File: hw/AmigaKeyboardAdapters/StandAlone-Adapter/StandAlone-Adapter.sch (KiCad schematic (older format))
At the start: 52 parts, among them J1 RJ10, J2 Conn_02x03_Odd_Even, P1 CONN_01X02, Q1 BSS138, Q2 BSS138, Q3 BSS138, U1 AZ1117-3.3, U3 STM32F401RCTx

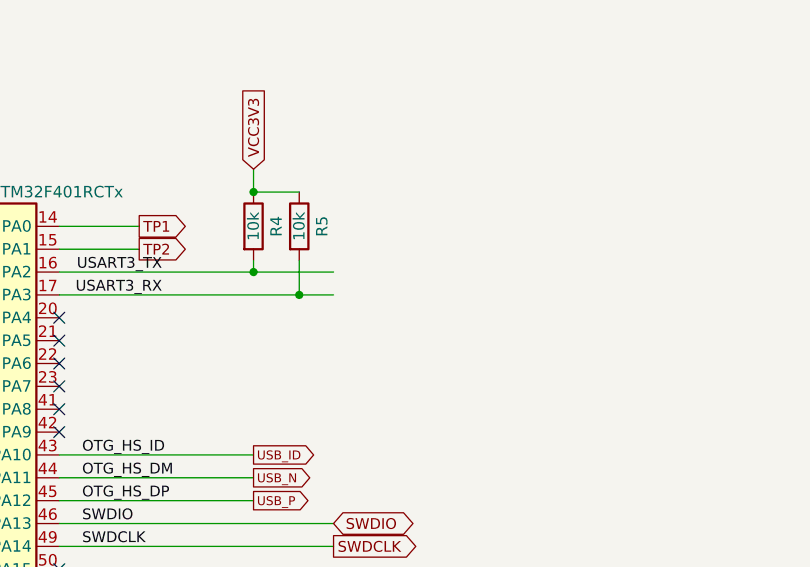
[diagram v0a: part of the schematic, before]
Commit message: The Debug UART Pins (RX & TX) were left unconnected
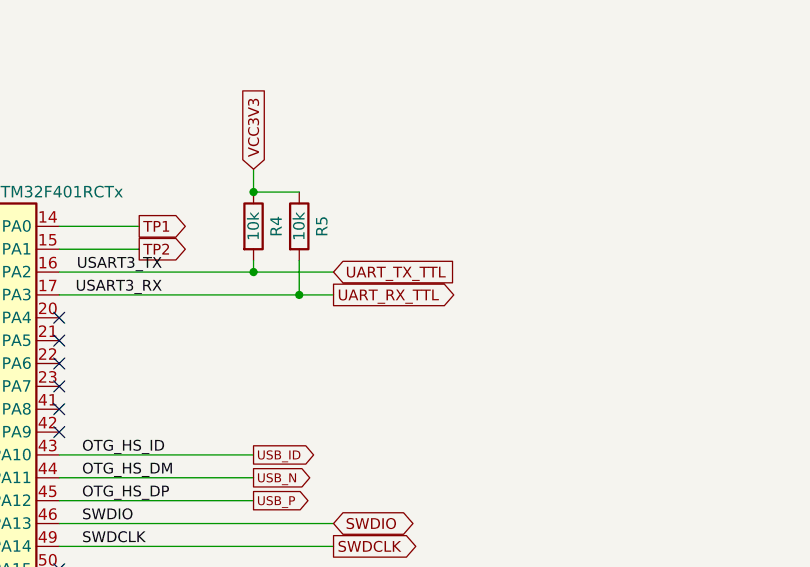
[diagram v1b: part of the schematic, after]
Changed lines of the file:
@@
 Wire Notes Line
 	10600 3600 10600 2600
+Text GLabel 10450 4800 2    47   Input ~ 0
+UART_TX_TTL
+Text GLabel 10450 4900 2    47   Output ~ 0
+UART_RX_TTL
 $EndSCHEMATC

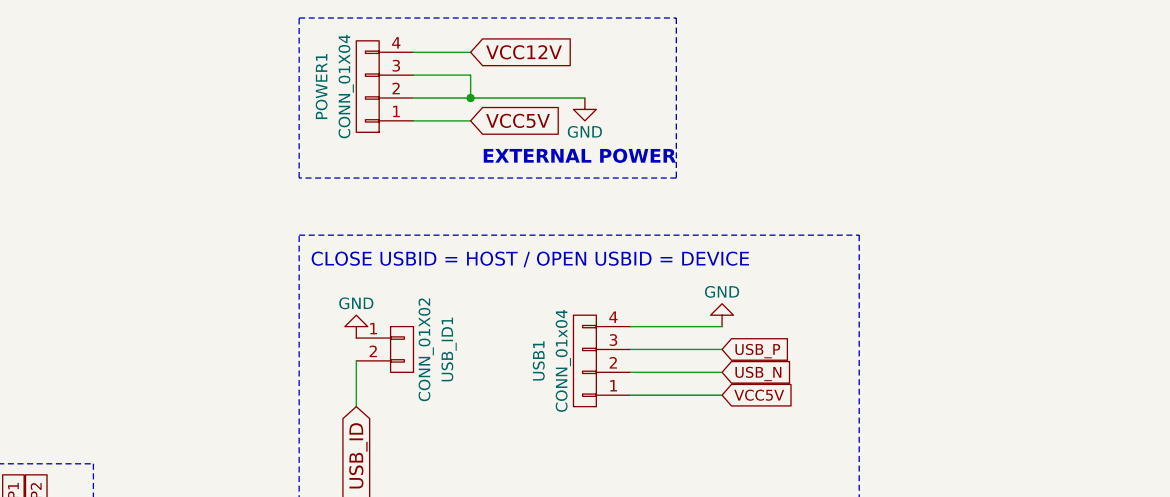
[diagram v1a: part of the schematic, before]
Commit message: Changed to reflect new path on my system
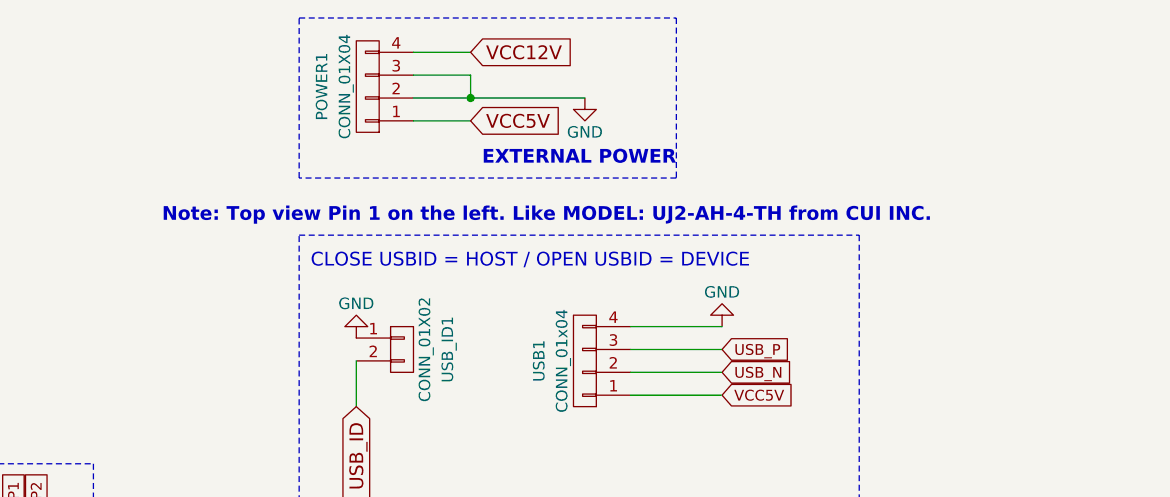
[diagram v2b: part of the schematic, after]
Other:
- note added: "Note: Top view Pin 1 on the left. Like MODEL: UJ2-AH-4-TH from CUI INC."
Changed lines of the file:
@@
 Text GLabel 10450 4900 2    47   Output ~ 0
 UART_RX_TTL
+Text Notes 12450 1550 0    60   ~ 12
+Note: Top view Pin 1 on the left. Like MODEL: UJ2-AH-4-TH from CUI INC.
 $EndSCHEMATC

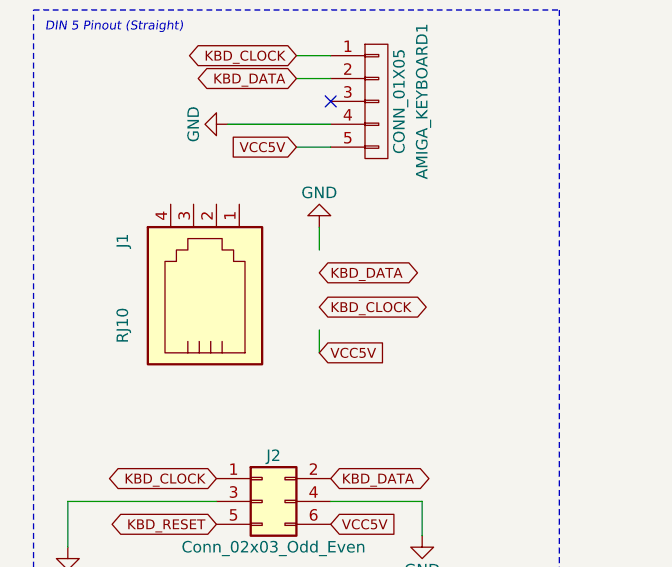
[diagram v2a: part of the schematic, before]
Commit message: Added all kicad libraries
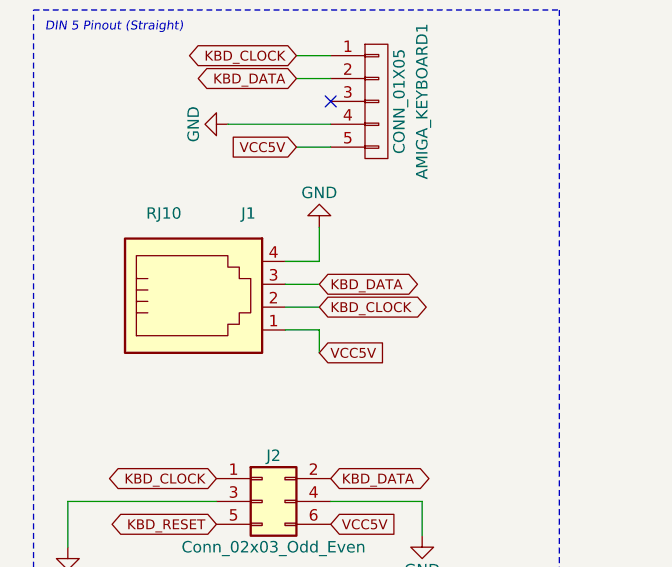
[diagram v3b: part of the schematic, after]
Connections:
- wire segments 105 -> 109
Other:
- moved on the sheet: J1
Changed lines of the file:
@@
 LIBS:Timer
 LIBS:Switch
-LIBS:StandAlone-Adapter-cache
 LIBS:AmigaComponents
+LIBS:4xxx
+LIBS:4xxx_IEEE
+LIBS:74xGxx
+LIBS:74xx_IEEE
+LIBS:Amplifier_Audio
+LIBS:Amplifier_Buffer
+LIBS:Amplifier_Current
+LIBS:Amplifier_Difference
+LIBS:Amplifier_Instrumentation
+LIBS:Amplifier_Operational
+LIBS:Amplifier_Video
+LIBS:Analog
+LIBS:Analog_ADC
+LIBS:Analog_DAC
+LIBS:Analog_Switch
+LIBS:Audio
+LIBS:Battery_Management
+LIBS:Comparator
+LIBS:Connector
+LIBS:Connector_Generic
+LIBS:Connector_Generic_MountingPin
+LIBS:Connector_Generic_Shielded
+LIBS:Converter_ACDC
+LIBS:Converter_DCDC
+LIBS:CPLD_Altera
+LIBS:CPLD_Xilinx
+LIBS:CPU
+LIBS:CPU_NXP_6800
+LIBS:CPU_NXP_68000
+LIBS:CPU_PowerPC
+LIBS:Device
+LIBS:Diode
+LIBS:Diode_Bridge
+LIBS:Diode_Laser
+LIBS:Display_Character
+LIBS:Display_Graphic
+LIBS:Driver_Display
+LIBS:Driver_FET
+LIBS:Driver_LED
+LIBS:Driver_Motor
+LIBS:Driver_Relay
+LIBS:DSP_AnalogDevices
+LIBS:DSP_Freescale
+LIBS:DSP_Microchip_DSPIC33
+LIBS:DSP_Motorola
+LIBS:DSP_Texas
+LIBS:Fiber_Optic
+LIBS:Filter
+LIBS:FPGA_Lattice
+LIBS:FPGA_Microsemi
+LIBS:FPGA_Xilinx
+LIBS:FPGA_Xilinx_Artix7
+LIBS:FPGA_Xilinx_Kintex7
+LIBS:FPGA_Xilinx_Spartan6
+LIBS:FPGA_Xilinx_Virtex5
+LIBS:FPGA_Xilinx_Virtex6
+LIBS:FPGA_Xilinx_Virtex7
+LIBS:ft232rl
+LIBS:GPU
+LIBS:Graphic
+LIBS:Interface
+LIBS:Interface_CAN_LIN
+LIBS:Interface_CurrentLoop
+LIBS:Interface_Ethernet
+LIBS:Interface_Expansion
+LIBS:Interface_HID
+LIBS:Interface_LineDriver
+LIBS:Interface_Optical
+LIBS:Interface_Telecom
+LIBS:Interface_UART
+LIBS:Interface_USB
+LIBS:Isolator
+LIBS:Isolator_Analog
+LIBS:Jumper
+LIBS:LED
+LIBS:Logic_LevelTranslator
+LIBS:Logic_Programmable
+LIBS:MCU_AnalogDevices
+LIBS:MCU_Cypress
+LIBS:MCU_Espressif
+LIBS:MCU_Intel
+LIBS:MCU_Microchip_8051
+LIBS:MCU_Microchip_ATmega
+LIBS:MCU_Microchip_ATtiny
+LIBS:MCU_Microchip_AVR
+LIBS:MCU_Microchip_PIC10
+LIBS:MCU_Microchip_PIC12
+LIBS:MCU_Microchip_PIC16
+LIBS:MCU_Microchip_PIC18
+LIBS:MCU_Microchip_PIC24
+LIBS:MCU_Microchip_PIC32
+LIBS:MCU_Microchip_SAMD
+LIBS:MCU_Microchip_SAME
+LIBS:MCU_Microchip_SAML
+LIBS:MCU_Module
+LIBS:MCU_Nordic
+LIBS:MCU_NXP_ColdFire
+LIBS:MCU_NXP_HC11
+LIBS:MCU_NXP_HC12
+LIBS:MCU_NXP_HCS12
+LIBS:MCU_NXP_Kinetis
+LIBS:MCU_NXP_LPC
+LIBS:MCU_NXP_MAC7100
+LIBS:MCU_NXP_MCore
+LIBS:MCU_NXP_S08
+LIBS:MCU_Parallax
+LIBS:MCU_SiFive
+LIBS:MCU_SiliconLabs
+LIBS:MCU_ST_STM8
+LIBS:MCU_ST_STM32F0
+LIBS:MCU_ST_STM32F1
+LIBS:MCU_ST_STM32F2
+LIBS:MCU_ST_STM32F3
+LIBS:MCU_ST_STM32F4
+LIBS:MCU_ST_STM32F7
+LIBS:MCU_ST_STM32H7
+LIBS:MCU_ST_STM32L0
+LIBS:MCU_ST_STM32L1
+LIBS:MCU_ST_STM32L4
+LIBS:MCU_ST_STM32L4+
+LIBS:MCU_Texas
+LIBS:MCU_Texas_MSP430
+LIBS:Mechanical
+LIBS:Memory_Controller
+LIBS:Memory_EEPROM
+LIBS:Memory_EPROM
+LIBS:Memory_Flash
+LIBS:Memory_NVRAM
+LIBS:Memory_RAM
+LIBS:Memory_ROM
+LIBS:Memory_UniqueID
+LIBS:Motor
+LIBS:Oscillator
+LIBS:Potentiometer_Digital
+LIBS:Power_Management
+LIBS:Power_Protection
+LIBS:Power_Supervisor
+LIBS:pspice
+LIBS:Reference_Current
+LIBS:Reference_Voltage
+LIBS:Regulator_Controller
+LIBS:Regulator_Current
+LIBS:Regulator_Linear
+LIBS:Regulator_SwitchedCapacitor
+LIBS:Regulator_Switching
+LIBS:Relay
+LIBS:Relay_SolidState
+LIBS:RF
+LIBS:RF_AM_FM
+LIBS:RF_Amplifier
+LIBS:RF_Bluetooth
+LIBS:RF_GPS
+LIBS:RF_GSM
+LIBS:RF_Mixer
+LIBS:RF_Module
+LIBS:RF_RFID
+LIBS:RF_Switch
+LIBS:RF_WiFi
+LIBS:RF_ZigBee
+LIBS:Security
+LIBS:Sensor
+LIBS:Sensor_Audio
+LIBS:Sensor_Current
+LIBS:Sensor_Gas
+LIBS:Sensor_Humidity
+LIBS:Sensor_Magnetic
+LIBS:Sensor_Motion
+LIBS:Sensor_Optical
+LIBS:Sensor_Pressure
+LIBS:Sensor_Proximity
+LIBS:Sensor_Temperature
+LIBS:Sensor_Touch
+LIBS:Sensor_Voltage
 EELAYER 25 0
 EELAYER END
@@
 Text GLabel 2050 9450 2    43   BiDi ~ 0
 KBD_CLOCK
-Text GLabel 2050 9300 2    43   BiDi ~ 0
-KBD_DATA
 $Comp
 L GND #PWR023
@@
 L RJ10 J1
 U 1 1 5C1EBC98
-P 1600 9400
-F 0 "J1" H 1840 9810 50  0000 C CNN
-F 1 "RJ10" H 1470 9810 50  0000 C CNN
-F 2 "RetroBitLab:RJ10-RECEPTACLE-Assmann-ASS-2004-3-4-LP-N-R" H 1600 9400 50  0001 C CNN
-F 3 "" H 1600 9400 50  0000 C CNN
-	1    1600 9400
-	0    -1   -1   0
-$EndComp
-Wire Wire Line
-	2050 9100 2050 9200
+P 1500 9450
+F 0 "J1" H 1740 9860 50  0000 C CNN
+F 1 "RJ10" H 1370 9860 50  0000 C CNN
+F 2 "RetroBitLab:RJ10-RECEPTACLE-Assmann-ASS-2004-3-4-LP-N-R" H 1500 9450 50  0001 C CNN
+F 3 "" H 1500 9450 50  0000 C CNN
+	1    1500 9450
+	1    0    0    -1
+$EndComp
 Wire Wire Line
 	2050 9550 2050 9650
@@
 Text Notes 12450 1550 0    60   ~ 12
 Note: Top view Pin 1 on the left. Like MODEL: UJ2-AH-4-TH from CUI INC.
+Text GLabel 2050 9350 2    43   BiDi ~ 0
+KBD_DATA
+Wire Wire Line
+	1900 9250 2050 9250
+Wire Wire Line
+	2050 9250 2050 9100
+Wire Wire Line
+	2050 9350 1900 9350
+Wire Wire Line
+	2050 9450 1900 9450
+Wire Wire Line
+	1900 9550 2050 9550
 $EndSCHEMATC

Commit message: added filled zone and changed footprint for button reset
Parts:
- RESET1: footprint Buttons_Switches_SMD:SW_SPST_FSMSM -> RetroBitLab:SW_SPST_FSMSM_3D
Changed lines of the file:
@@
 LIBS:Sensor_Touch
 LIBS:Sensor_Voltage
+LIBS:StandAlone-Adapter-cache
 EELAYER 25 0
 EELAYER END
@@
 F 0 "RESET1" H 7200 4450 50  0000 C CNN
 F 1 "SW_PUSH" H 7200 4220 50  0000 C CNN
-F 2 "Buttons_Switches_SMD:SW_SPST_FSMSM" H 7200 4300 50  0001 C CNN
+F 2 "RetroBitLab:SW_SPST_FSMSM_3D" H 7200 4300 50  0001 C CNN
 F 3 "" H 7200 4300 50  0000 C CNN
 	1    7200 4300

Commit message: modified for IDC Connector
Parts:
- J2: footprint Pin_Headers:Pin_Header_Straight_2x03 -> Connector_IDC:IDC-Header_2x03_P2.54mm_Vertical
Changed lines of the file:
@@
 F 0 "J2" H 1850 10500 50  0000 C CNN
 F 1 "Conn_02x03_Odd_Even" H 1850 10100 50  0000 C CNN
-F 2 "Pin_Headers:Pin_Header_Straight_2x03" H 1800 10300 50  0001 C CNN
+F 2 "Connector_IDC:IDC-Header_2x03_P2.54mm_Vertical" H 1800 10300 50  0001 C CNN
 F 3 "" H 1800 10300 50  0001 C CNN
 	1    1800 10300

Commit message: REfactoring for new Crystal Oscillator & new 1208 footprints handsoldering
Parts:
- C4, C5, C6, C7, C8, C9: footprint Capacitors_SMD:C_0603_HandSoldering -> Capacitors_SMD:C_1206_HandSoldering
- D1, D2, D3, D4: footprint LEDs:LED_0603 -> LEDs:LED_1206
- J2: footprint Connector_IDC:IDC-Header_2x03_P2.54mm_Vertical -> RetroBitLab:IDC-Header_2x03_P2.54mm_Vertical
- R1, R10, R11, R12, R13, R2, R3, R4, R5, R6, R7, R8, R9: footprint Resistors_SMD:R_0603_HandSoldering -> Resistors_SMD:R_1206_HandSoldering
- XT1: footprint Crystals:Crystal_SMD_0603_4Pads -> RetroBitLab:Crystal_HC49-4H_Vertical_3D
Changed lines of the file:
@@
 LIBS:MCU_Texas_MSP430
 LIBS:Mechanical
-LIBS:Memory_Controller
 LIBS:Memory_EEPROM
 LIBS:Memory_EPROM
@@
 F 0 "XT1" H 7200 5900 50  0000 C CNN
 F 1 "8Mhz" H 7200 5600 50  0000 C CNN
-F 2 "Crystals:Crystal_SMD_0603_4Pads" H 7200 5750 50  0001 C CNN
+F 2 "RetroBitLab:Crystal_HC49-4H_Vertical_3D" H 7200 5750 50  0001 C CNN
 F 3 "" H 7200 5750 50  0000 C CNN
 	1    7200 5750
@@
 F 0 "C4" H 6825 5550 50  0000 L CNN
 F 1 "22p" H 6825 5350 50  0000 L CNN
-F 2 "Capacitors_SMD:C_0603_HandSoldering" H 6838 5300 50  0001 C CNN
+F 2 "Capacitors_SMD:C_1206_HandSoldering" H 6838 5300 50  0001 C CNN
 F 3 "" H 6800 5450 50  0000 C CNN
 	1    6800 5450
@@
 F 0 "C5" H 6825 6150 50  0000 L CNN
 F 1 "22p" H 6825 5950 50  0000 L CNN
-F 2 "Capacitors_SMD:C_0603_HandSoldering" H 6838 5900 50  0001 C CNN
+F 2 "Capacitors_SMD:C_1206_HandSoldering" H 6838 5900 50  0001 C CNN
 F 3 "" H 6800 6050 50  0000 C CNN
 	1    6800 6050
@@
 F 0 "C6" H 7875 3600 50  0000 L CNN
 F 1 "100n" H 7875 3400 50  0000 L CNN
-F 2 "Capacitors_SMD:C_0603_HandSoldering" H 7888 3350 50  0001 C CNN
+F 2 "Capacitors_SMD:C_1206_HandSoldering" H 7888 3350 50  0001 C CNN
 F 3 "" H 7850 3500 50  0000 C CNN
 	1    7850 3500
@@
 F 0 "C7" H 8125 3600 50  0000 L CNN
 F 1 "100n" H 8125 3400 50  0000 L CNN
-F 2 "Capacitors_SMD:C_0603_HandSoldering" H 8138 3350 50  0001 C CNN
+F 2 "Capacitors_SMD:C_1206_HandSoldering" H 8138 3350 50  0001 C CNN
 F 3 "" H 8100 3500 50  0000 C CNN
 	1    8100 3500
@@
 F 0 "C8" H 8375 3600 50  0000 L CNN
 F 1 "100n" H 8375 3400 50  0000 L CNN
-F 2 "Capacitors_SMD:C_0603_HandSoldering" H 8388 3350 50  0001 C CNN
+F 2 "Capacitors_SMD:C_1206_HandSoldering" H 8388 3350 50  0001 C CNN
 F 3 "" H 8350 3500 50  0000 C CNN
 	1    8350 3500
@@
 F 0 "C9" H 8625 3600 50  0000 L CNN
 F 1 "100n" H 8625 3400 50  0000 L CNN
-F 2 "Capacitors_SMD:C_0603_HandSoldering" H 8638 3350 50  0001 C CNN
+F 2 "Capacitors_SMD:C_1206_HandSoldering" H 8638 3350 50  0001 C CNN
 F 3 "" H 8600 3500 50  0000 C CNN
 	1    8600 3500
@@
 F 0 "R4" V 10200 4600 50  0000 C CNN
 F 1 "10k" V 10100 4600 50  0000 C CNN
-F 2 "Resistors_SMD:R_0603_HandSoldering" V 10030 4600 50  0001 C CNN
+F 2 "Resistors_SMD:R_1206_HandSoldering" V 10030 4600 50  0001 C CNN
 F 3 "" H 10100 4600 50  0000 C CNN
 	1    10100 4600
@@
 F 0 "R5" V 10400 4600 50  0000 C CNN
 F 1 "10k" V 10300 4600 50  0000 C CNN
-F 2 "Resistors_SMD:R_0603_HandSoldering" V 10230 4600 50  0001 C CNN
+F 2 "Resistors_SMD:R_1206_HandSoldering" V 10230 4600 50  0001 C CNN
 F 3 "" H 10300 4600 50  0000 C CNN
 	1    10300 4600
@@
 F 0 "R3" V 7730 4100 50  0000 C CNN
 F 1 "10K" V 7650 4100 50  0000 C CNN
-F 2 "Resistors_SMD:R_0603_HandSoldering" V 7580 4100 50  0001 C CNN
+F 2 "Resistors_SMD:R_1206_HandSoldering" V 7580 4100 50  0001 C CNN
 F 3 "" H 7650 4100 50  0000 C CNN
 	1    7650 4100
@@
 F 0 "R2" V 3350 5600 50  0000 C CNN
 F 1 "220" V 3250 5600 50  0000 C CNN
-F 2 "Resistors_SMD:R_0603_HandSoldering" V 3180 5600 50  0001 C CNN
+F 2 "Resistors_SMD:R_1206_HandSoldering" V 3180 5600 50  0001 C CNN
 F 3 "" H 3250 5600 50  0000 C CNN
 	1    3250 5600
@@
 F 0 "D2" H 3250 6050 50  0000 C CNN
 F 1 "LED" H 3250 5850 50  0000 C CNN
-F 2 "LEDs:LED_0603" H 3250 5950 50  0001 C CNN
+F 2 "LEDs:LED_1206" H 3250 5950 50  0001 C CNN
 F 3 "" H 3250 5950 50  0000 C CNN
 	1    3250 5950
@@
 F 0 "D1" H 1250 6050 50  0000 C CNN
 F 1 "LED" H 1250 5850 50  0000 C CNN
-F 2 "LEDs:LED_0603" H 1250 5950 50  0001 C CNN
+F 2 "LEDs:LED_1206" H 1250 5950 50  0001 C CNN
 F 3 "" H 1250 5950 50  0000 C CNN
 	1    1250 5950
@@
 F 0 "R1" V 1330 5600 50  0000 C CNN
 F 1 "330" V 1250 5600 50  0000 C CNN
-F 2 "Resistors_SMD:R_0603_HandSoldering" V 1180 5600 50  0001 C CNN
+F 2 "Resistors_SMD:R_1206_HandSoldering" V 1180 5600 50  0001 C CNN
 F 3 "" H 1250 5600 50  0000 C CNN
 	1    1250 5600
@@
 F 0 "D3" H 1950 3150 50  0000 C CNN
 F 1 "LED" H 1950 2950 50  0000 C CNN
-F 2 "LEDs:LED_0603" H 1950 3050 50  0001 C CNN
+F 2 "LEDs:LED_1206" H 1950 3050 50  0001 C CNN
 F 3 "" H 1950 3050 50  0000 C CNN
 	1    1950 3050
@@
 F 0 "R6" V 2030 2700 50  0000 C CNN
 F 1 "1K" V 1950 2700 50  0000 C CNN
-F 2 "Resistors_SMD:R_0603_HandSoldering" V 1880 2700 50  0001 C CNN
+F 2 "Resistors_SMD:R_1206_HandSoldering" V 1880 2700 50  0001 C CNN
 F 3 "" H 1950 2700 50  0000 C CNN
 	1    1950 2700
@@
 F 0 "R7" V 13980 5800 50  0000 C CNN
 F 1 "10k" V 13900 5800 50  0000 C CNN
-F 2 "Resistors_SMD:R_0603_HandSoldering" V 13830 5800 50  0001 C CNN
+F 2 "Resistors_SMD:R_1206_HandSoldering" V 13830 5800 50  0001 C CNN
 F 3 "" H 13900 5800 50  0000 C CNN
 	1    13900 5800
@@
 F 0 "R8" V 14480 5800 50  0000 C CNN
 F 1 "10k" V 14400 5800 50  0000 C CNN
-F 2 "Resistors_SMD:R_0603_HandSoldering" V 14330 5800 50  0001 C CNN
+F 2 "Resistors_SMD:R_1206_HandSoldering" V 14330 5800 50  0001 C CNN
 F 3 "" H 14400 5800 50  0000 C CNN
 	1    14400 5800
@@
 F 0 "R9" V 13980 8150 50  0000 C CNN
 F 1 "10k" V 13900 8150 50  0000 C CNN
-F 2 "Resistors_SMD:R_0603_HandSoldering" V 13830 8150 50  0001 C CNN
+F 2 "Resistors_SMD:R_1206_HandSoldering" V 13830 8150 50  0001 C CNN
 F 3 "" H 13900 8150 50  0000 C CNN
 	1    13900 8150
@@
 F 0 "R10" V 14480 8150 50  0000 C CNN
 F 1 "10k" V 14400 8150 50  0000 C CNN
-F 2 "Resistors_SMD:R_0603_HandSoldering" V 14330 8150 50  0001 C CNN
+F 2 "Resistors_SMD:R_1206_HandSoldering" V 14330 8150 50  0001 C CNN
 F 3 "" H 14400 8150 50  0000 C CNN
 	1    14400 8150
@@
 F 0 "R11" V 13980 7000 50  0000 C CNN
 F 1 "10k" V 13900 7000 50  0000 C CNN
-F 2 "Resistors_SMD:R_0603_HandSoldering" V 13830 7000 50  0001 C CNN
+F 2 "Resistors_SMD:R_1206_HandSoldering" V 13830 7000 50  0001 C CNN
 F 3 "" H 13900 7000 50  0000 C CNN
 	1    13900 7000
@@
 F 0 "R12" V 14480 7000 50  0000 C CNN
 F 1 "10k" V 14400 7000 50  0000 C CNN
-F 2 "Resistors_SMD:R_0603_HandSoldering" V 14330 7000 50  0001 C CNN
+F 2 "Resistors_SMD:R_1206_HandSoldering" V 14330 7000 50  0001 C CNN
 F 3 "" H 14400 7000 50  0000 C CNN
 	1    14400 7000
@@
 F 0 "R13" V 11730 3050 50  0000 C CNN
 F 1 "330" V 11650 3050 50  0000 C CNN
-F 2 "Resistors_SMD:R_0603_HandSoldering" V 11580 3050 50  0001 C CNN
+F 2 "Resistors_SMD:R_1206_HandSoldering" V 11580 3050 50  0001 C CNN
 F 3 "" H 11650 3050 50  0000 C CNN
 	1    11650 3050
@@
 F 0 "D4" H 11300 3150 50  0000 C CNN
 F 1 "LED" H 11300 2950 50  0000 C CNN
-F 2 "LEDs:LED_0603" H 11300 3050 50  0001 C CNN
+F 2 "LEDs:LED_1206" H 11300 3050 50  0001 C CNN
 F 3 "" H 11300 3050 50  0000 C CNN
 	1    11300 3050
@@
 F 0 "J2" H 1850 10500 50  0000 C CNN
 F 1 "Conn_02x03_Odd_Even" H 1850 10100 50  0000 C CNN
-F 2 "Connector_IDC:IDC-Header_2x03_P2.54mm_Vertical" H 1800 10300 50  0001 C CNN
+F 2 "RetroBitLab:IDC-Header_2x03_P2.54mm_Vertical" H 1800 10300 50  0001 C CNN
 F 3 "" H 1800 10300 50  0001 C CNN
 	1    1800 10300

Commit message: Modified for Capacitors & Added some boot options
Replaced Electrolitic Capacitors with Tantalum ones. Added some
capacitor as in the evaluation board schematics. Added BOOT1 pin. Added
resistors for USB D+ D- lines. Increased the GND trace size to 0.35.
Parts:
- removed C3: 47u, Capacitors_SMD:c_elec_4x4.5, symbol CP1
- removed L1: 10uH, Inductors:SELF-WE-PD3S, symbol INDUCTOR
- removed L2: 10uH, Inductors:SELF-WE-PD3S, symbol INDUCTOR_SMALL
- removed R3: 10K, Resistors_SMD:R_1206_HandSoldering, symbol R
- added BOOT1: CONN_01X03, Pin_Headers:Pin_Header_Straight_1x03, symbol CONN_01X03
- added C10, C12, C14, C3: 100n, Capacitors_SMD:C_1206_HandSoldering, symbol C_Small
- added C11: 10u, Capacitors_Tantalum_SMD:TantalC_SizeA_EIA-3216_HandSoldering, symbol CP1_Small
- added C13: 4.7u, Capacitors_SMD:C_1206_HandSoldering, symbol C_Small
- added R14, R15: 10K, Resistors_SMD:R_1206_HandSoldering, symbol R_Small
- added R16, R17: 12, Resistors_SMD:R_1206_HandSoldering, symbol R_Small
- added R3: 22K, Resistors_SMD:R_1206_HandSoldering, symbol R_Small
- C1, C2: footprint Capacitors_SMD:c_elec_4x4.5 -> Capacitors_Tantalum_SMD:TantalC_SizeA_EIA-3216_HandSoldering
- R1, R13: value 330 -> 1.5K
- R10, R11, R12, R4, R5, R7, R8, R9: value 10k -> 10K
- R2: value 220 -> 1.5K
- R6: value 1K -> 1.5K
- renumbered BOOT1 to BOOT0
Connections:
- net labels added: BOOT1, NRST, VDDA, VSSA
- wire segments 109 -> 132
- no-connect marks 74 -> 72
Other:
- note added: "BOOT SELECTION"
- note added: "INTERNAL VOLTAGE STABILIZER"
- note removed: "BOOT SELECTOR"
- moved on the sheet: D2, D4, EN1, R13, R2, RESET1, TP1/1
